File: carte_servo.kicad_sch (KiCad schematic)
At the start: 37 parts, among them J16 Conn_01x04_Male, J17 Conn_01x04_Male, J2 Conn_02x04_Top_Bottom, J24 Conn_LEDs, P1 USB_C_Plug_USB2.0, SW1 CK_KMS2xxG, U1 XGZP6897D_differential_pressu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, U2 XGZP6897D_differential_pressu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, U6 SN65HVD230, U7 LD1117S33TR_SOT223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

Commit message: small stuff
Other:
- sheet Servos ports: added GND; removed GND_SERVO
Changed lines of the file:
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@@
 	(label "Pressure_2"
 		(at 83.82 127 180)
-		(fields_autoplaced yes)
 		(effects
 			(font
@@
 	(label "Pressure_1"
 		(at 82.55 100.33 180)
-		(fields_autoplaced yes)
 		(effects
 			(font
@@
 			)
 		)
-		(pin "GND_SERVO" input
-			(at 257.81 46.99 270)
+		(pin "SERVO_POWER_1" input
+			(at 226.06 38.1 180)
 			(effects
 				(font
@@
 			)
 		)
-		(pin "SERVO_POWER_1" input
-			(at 226.06 38.1 180)
+		(pin "GND" input
+			(at 257.81 46.99 270)
 			(effects
 				(font

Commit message: add DCDC 5V
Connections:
- no-connect marks 7 -> 8
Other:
- added sheet DCDC_5V (DCDC_5V.kicad_sch)
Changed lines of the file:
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@@
 	)
 	(no_connect
+		(at 312.42 101.6)
+	)
+	(no_connect
 		(at 38.1 63.5)
 	)
@@
 	(wire
 		(pts
+			(xy 344.17 109.22) (xy 344.17 107.95)
+		)
+		(stroke
+			(width 0)
+			(type default)
+		)
+	)
+	(wire
+		(pts
 			(xy 111.76 86.36) (xy 111.76 95.25)
 		)
@@
 	(wire
 		(pts
+			(xy 356.87 97.79) (xy 353.06 97.79)
+		)
+		(stroke
+			(width 0)
+			(type default)
+		)
+	)
+	(wire
+		(pts
 			(xy 93.98 113.03) (xy 87.63 113.03)
 		)
@@
 	(wire
 		(pts
+			(xy 308.61 95.25) (xy 312.42 95.25)
+		)
+		(stroke
+			(width 0)
+			(type default)
+		)
+	)
+	(wire
+		(pts
 			(xy 210.82 50.8) (xy 210.82 53.34)
 		)
@@
 		)
 	)
+	(global_label "5V"
+		(shape output)
+		(at 356.87 97.79 0)
+		(fields_autoplaced yes)
+		(effects
+			(font
+				(size 1.27 1.27)
+			)
+			(justify left)
+		)
+		(property "Intersheetrefs" "${INTERSHEET_REFS}"
+			(at 362.1533 97.79 0)
+			(effects
+				(font
+					(size 1.27 1.27)
+				)
+				(justify left)
+				(hide yes)
+			)
+		)
+	)
 	(global_label "SDA"
 		(shape bidirectional)
@@
 	(global_label "GND"
 		(shape input)
+		(at 344.17 109.22 270)
+		(fields_autoplaced yes)
+		(effects
+			(font
+				(size 1.27 1.27)
+			)
+			(justify right)
+		)
+		(property "Intersheetrefs" "${INTERSHEET_REFS}"
+			(at 344.17 116.0757 90)
+			(effects
+				(font
+					(size 1.27 1.27)
+				)
+				(justify right)
+				(hide yes)
+			)
+		)
+	)
+	(global_label "GND"
+		(shape input)
 		(at 115.57 121.92 0)
 		(fields_autoplaced yes)
@@
 		)
 	)
+	(global_label "BATT_12V"
+		(shape input)
+		(at 308.61 95.25 180)
+		(fields_autoplaced yes)
+		(effects
+			(font
+				(size 1.27 1.27)
+			)
+			(justify right)
+		)
+		(property "Intersheetrefs" "${INTERSHEET_REFS}"
+			(at 296.8558 95.25 0)
+			(effects
+				(font
+					(size 1.27 1.27)
+				)
+				(justify right)
+				(hide yes)
+			)
+		)
+	)
 	(global_label "SERVO_1"
 		(shape output)
@@
 				)
 			)
+		)
+	)
+	(sheet
+		(at 312.42 90.17)
+		(size 40.64 17.78)
+		(fields_autoplaced yes)
+		(stroke
+			(width 0.1524)
+			(type solid)
+		)
+		(fill
+			(color 0 0 0 0.0000)
+		)
+		(property "Sheetname" "DCDC_5V"
+			(at 312.42 89.4584 0)
+			(effects
+				(font
+					(size 1.27 1.27)
+				)
+				(justify left bottom)
+			)
+		)
+		(property "Sheetfile" "DCDC_5V.kicad_sch"
+			(at 312.42 108.5346 0)
+			(effects
+				(font
+					(size 1.27 1.27)
+				)
+				(justify left top)
+			)
+		)
+		(pin "Vin" input
+			(at 312.42 95.25 180)
+			(effects
+				(font
+					(size 1.27 1.27)
+				)
+				(justify left)
+			)
+		)
+		(pin "GND" input
+			(at 344.17 107.95 270)
+			(effects
+				(font
+					(size 1.27 1.27)
+				)
+				(justify left)
+			)
+		)
+		(pin "enable" input
+			(at 312.42 101.6 180)
+			(effects
+				(font
+					(size 1.27 1.27)
+				)
+				(justify left)
+			)
+		)
+		(pin "Vout_5V" output
+			(at 353.06 97.79 0)
+			(effects
+				(font
+					(size 1.27 1.27)
+				)
+				(justify right)
+			)
+		)
+		(instances
+			(project "carte_servo"
+				(path "/e63e39d7-6ac0-4ffd-8aa3-1841a4541b55"
+					(page "9")
+				)
+			)

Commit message: add ESD diodes for USB
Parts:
- added D2, D3: ESD321, Diode_SMD:D_SOD-523, symbol Device:D_Zener
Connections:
- net D+: now also D2.1 (K)
- net D-: now also D3.1 (K)
- net GND: now also D2.2 (A), D3.2 (A)
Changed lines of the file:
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@@
 	)
 	(junction
+		(at 613.41 54.61)
+		(diameter 0)
+		(color 0 0 0 0)
+	)
+	(junction
 		(at 229.87 53.34)
 		(diameter 0)
@@
 	(wire
 		(pts
-			(xy 109.22 153.67) (xy 111.76 153.67)
+			(xy 593.09 41.91) (xy 598.17 41.91)
 		)
 		(stroke
@@
 	(wire
 		(pts
-			(xy 314.96 10.16) (xy 331.47 10.16)
+			(xy 109.22 153.67) (xy 111.76 153.67)
 		)
 		(stroke
@@
 	(wire
 		(pts
-			(xy 171.45 34.29) (xy 179.07 34.29)
+			(xy 314.96 10.16) (xy 331.47 10.16)
 		)
 		(stroke
@@
 	(wire
 		(pts
-			(xy 391.16 31.75) (xy 396.24 31.75)
+			(xy 171.45 34.29) (xy 179.07 34.29)
 		)
 		(stroke
@@
 	(wire
 		(pts
-			(xy 593.09 36.83) (xy 598.17 36.83)
+			(xy 391.16 31.75) (xy 396.24 31.75)
 		)
 		(stroke
@@
 	(wire
 		(pts
+			(xy 593.09 36.83) (xy 598.17 36.83)
+		)
+		(stroke
+			(width 0)
+			(type default)
+		)
+	)
+	(wire
+		(pts
 			(xy 391.16 82.55) (xy 396.24 82.55)
 		)
@@
 	(wire
 		(pts
+			(xy 613.41 54.61) (xy 613.41 58.42)
+		)
+		(stroke
+			(width 0)
+			(type default)
+		)
+	)
+	(wire
+		(pts
 			(xy 608.33 31.75) (xy 608.33 36.83)
 		)
@@
 	(wire
 		(pts
+			(xy 607.06 54.61) (xy 613.41 54.61)
+		)
+		(stroke
+			(width 0)
+			(type default)
+		)
+	)
+	(wire
+		(pts
 			(xy 473.71 0) (xy 480.06 0)
 		)
@@
 	(wire
 		(pts
+			(xy 613.41 54.61) (xy 619.76 54.61)
+		)
+		(stroke
+			(width 0)
+			(type default)
+		)
+	)
+	(wire
+		(pts
 			(xy 111.76 86.36) (xy 111.76 95.25)
 		)
@@
 	(wire
 		(pts
-			(xy 593.09 41.91) (xy 598.17 41.91)
-		)
-		(stroke
-			(width 0)
-			(type default)
-		)
-	)
-	(wire
-		(pts
 			(xy 125.73 182.88) (xy 127 182.88)
 		)
@@
 		)
 	)
+	(global_label "D-"
+		(shape bidirectional)
+		(at 619.76 46.99 0)
+		(fields_autoplaced yes)
+		(effects
+			(font
+				(size 1.27 1.27)
+			)
+			(justify left)
+		)
+		(property "Intersheetrefs" "${INTERSHEET_REFS}"
+			(at 625.5876 46.99 0)
+			(effects
+				(font
+					(size 1.27 1.27)
+				)
+				(justify left)
+				(hide yes)
+			)
+		)
+	)
 	(global_label "ENABLE_SERVO_POWER_1"
 		(shape input)
@@
 		)
 	)
+	(global_label "GND"
+		(shape input)
+		(at 613.41 58.42 0)
+		(fields_autoplaced yes)
+		(effects
+			(font
+				(size 1.27 1.27)
+			)
+			(justify left)
+		)
+		(property "Intersheetrefs" "${INTERSHEET_REFS}"
+			(at 620.2657 58.42 0)
+			(effects
+				(font
+					(size 1.27 1.27)
+				)
+				(justify left)
+				(hide yes)
+			)
+		)
+	)
 	(global_label "GND_POWER"
 		(shape input)
@@
 		)
 	)
+	(global_label "D+"
+		(shape bidirectional)
+		(at 607.06 46.99 0)
+		(fields_autoplaced yes)
+		(effects
+			(font
+				(size 1.27 1.27)
+			)
+			(justify left)
+		)
+		(property "Intersheetrefs" "${INTERSHEET_REFS}"
+			(at 612.8876 46.99 0)
+			(effects
+				(font
+					(size 1.27 1.27)
+				)
+				(justify left)
+				(hide yes)
+			)
+		)
+	)
 	(global_label "3.3V"
 		(shape input)
@@
 	)
 	(symbol
+		(lib_id "Device:D_Zener")
+		(at 607.06 50.8 270)
+		(unit 1)
+		(exclude_from_sim no)
+		(in_bom yes)
+		(on_board yes)
+		(dnp no)
+		(fields_autoplaced yes)
+		(property "Reference" "D2"
+			(at 609.6 49.5299 90)
+			(effects
+				(font
+					(size 1.27 1.27)
+				)
+				(justify left)
+			)
+		)
+		(property "Value" "ESD321"
+			(at 609.6 52.0699 90)
+			(effects
+				(font
+					(size 1.27 1.27)
+				)
+				(justify left)
+			)
+		)
+		(property "Footprint" "Diode_SMD:D_SOD-523"
+			(at 607.06 50.8 0)
+			(effects
+				(font
+					(size 1.27 1.27)
+				)
+				(hide yes)
+			)
+		)
+		(property "Datasheet" "https://www.mouser.fr/ProductDetail/Texas-Instruments/ESD321DYAR?qs=rQFj71Wb1eXoYwRMra0IYA%3D%3D"
+			(at 607.06 50.8 0)
+			(effects
+				(font
+					(size 1.27 1.27)
+				)
+				(hide yes)
+			)
+		)
+		(property "Description" "Zener diode"
+			(at 607.06 50.8 0)
+			(effects
+				(font
+					(size 1.27 1.27)
+				)
+				(hide yes)
+			)
+		)
+		(pin "2"
+		)
+		(pin "1"
+		)
+		(instances
+			(project "carte_servo"
+				(path "/e63e39d7-6ac0-4ffd-8aa3-1841a4541b55"
+					(reference "D2")
+					(unit 1)
+				)
+			)
+		)
+	)
+	(symbol
 		(lib_id "Connector:Conn_01x04_Male")
 		(at 39.37 158.75 0)
@@
 					(unit 1)
 				)
+			)
+		)
+	)
+	(symbol
+		(lib_id "Device:D_Zener")
+		(at 619.76 50.8 270)
+		(unit 1)
+		(exclude_from_sim no)
+		(in_bom yes)
+		(on_board yes)
+		(dnp no)
+		(fields_autoplaced yes)
+		(property "Reference" "D3"
+			(at 622.3 49.5299 90)
+			(effects
+				(font
+					(size 1.27 1.27)
+				)
+				(justify left)
+			)
+		)
+		(property "Value" "ESD321"
+			(at 622.3 52.0699 90)
+			(effects
+				(font
+					(size 1.27 1.27)
+				)
+				(justify left)
+			)
+		)
+		(property "Footprint" "Diode_SMD:D_SOD-523"
+			(at 619.76 50.8 0)
+			(effects
+				(font
+					(size 1.27 1.27)
+				)
+				(hide yes)
+			)
+		)
+		(property "Datasheet" "https://www.mouser.fr/ProductDetail/Texas-Instruments/ESD321DYAR?qs=rQFj71Wb1eXoYwRMra0IYA%3D%3D"
+			(at 619.76 50.8 0)
+			(effects
+				(font
+					(size 1.27 1.27)
+				)
+				(hide yes)
+			)
+		)
+		(property "Description" "Zener diode"
+			(at 619.76 50.8 0)
+			(effects
+				(font
+					(size 1.27 1.27)
+				)
+				(hide yes)
+			)
+		)
+		(pin "2"
+		)
+		(pin "1"
+		)
+		(instances
+			(project "carte_servo"
+				(path "/e63e39d7-6ac0-4ffd-8aa3-1841a4541b55"
+					(reference "D3")
+					(unit 1)
+				)

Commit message: fix warnings + separate enable for Steppers
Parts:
- removed C8: C_Polarized, Capacitor_THT:CP_Radial_D10.0mm_P5.00mm, symbol Device:C_Polarized
- added R37: 0R, Resistor_SMD:R_0603_1608Metric, symbol Device:R_Small
- R12: value 0R -> NC
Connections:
- net ENABLE_SERVO_POWER_2 is gone; now on net ENABLE_SERVO_POWER_1: R12.1, U8.36 (U0RXD/GPIO44/CLK_OUT2)
- net ENABLE_SERVO_POWER_1: no longer R12.2
- net sense_5V: now also R37.2
- new net ENABLE_STEPPER_POWER: R12.2, R37.1
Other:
- note removed: "todo: générer du 5V"

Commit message: change fuse + start servo order + routing
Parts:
- F1: footprint Resistor_THT:R_Axial_DIN0411_L9.9mm_D3.6mm_P15.24mm_Horizontal -> Fuse:Fuse_Littelfuse-NANO2-451_453
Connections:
- net DIR_1: now also U8.20 (GPIO12/TOUCH12/ADC2_CH1/FSPICLK/FSPIIO6/SUBSPICLK); no longer U8.28 (SPIIO6/GPIO35/FSPID/SUBSPID)
- net DIR_2: now also U8.18 (GPIO10/TOUCH10/ADC1_CH9/FSPICS0/FSPIIO4/SUBSPICS0); no longer U8.31 (GPIO38/FSPIWP/SUBSPIWP)
- net LEDs: now also U8.6 (GPIO6/TOUCH6/ADC1_CH5); no longer U8.30 (SPIDQS/GPIO37/FSPIQ/SUBSPIQ)
- net SERVO_1: now also U8.34 (MTDI/GPIO41/CLK_OUT1); no longer U8.12 (GPIO8/TOUCH8/ADC1_CH7/SUBSPICS1)
- net SERVO_2: now also U8.28 (SPIIO6/GPIO35/FSPID/SUBSPID); no longer U8.18 (GPIO10/TOUCH10/ADC1_CH9/FSPICS0/FSPIIO4/SUBSPICS0)
- net SERVO_3: now also U8.30 (SPIDQS/GPIO37/FSPIQ/SUBSPIQ); no longer U8.19 (GPIO11/TOUCH11/ADC2_CH0/FSPID/FSPIIO5/SUBSPID)
- net SERVO_7: now also U8.29 (SPIIO7/GPIO36/FSPICLK/SUBSPICLK); no longer U8.20 (GPIO12/TOUCH12/ADC2_CH1/FSPICLK/FSPIIO6/SUBSPICLK)
- net SERVO_8: now also U8.37 (U0TXD/GPIO43/CLK_OUT1); no longer U8.6 (GPIO6/TOUCH6/ADC1_CH5), U8.9 (GPIO16/U0CTS/ADC2_CH5/XTAL_32K_N)
- net STEP_1: now also U8.12 (GPIO8/TOUCH8/ADC1_CH7/SUBSPICS1); no longer U8.29 (SPIIO7/GPIO36/FSPICLK/SUBSPICLK)
- net STEP_2: now also U8.19 (GPIO11/TOUCH11/ADC2_CH0/FSPID/FSPIIO5/SUBSPID); no longer U8.34 (MTDI/GPIO41/CLK_OUT1)
- net TRANSISTOR_3: now also U8.9 (GPIO16/U0CTS/ADC2_CH5/XTAL_32K_N); no longer U8.37 (U0TXD/GPIO43/CLK_OUT1)
- net CAN_H renamed CAN+
- net CAN_L renamed CAN-

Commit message: continue routing
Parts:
- added C8: 100nF, Capacitor_SMD:C_0603_1608Metric, symbol Device:C
- C11: value 100nF -> 4.7µF
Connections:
- net 3.3V: now also C11.1
- net GND: now also C8.2
- net Pressure_2: now also U8.38 (GPIO2/TOUCH2/ADC1_CH1), C8.1; no longer C11.1, U8.5 (GPIO5/TOUCH5/ADC1_CH4)
- net SERVO_1: now also U8.28 (SPIIO6/GPIO35/FSPID/SUBSPID); no longer U8.34 (MTDI/GPIO41/CLK_OUT1)
- net SERVO_2: now also U8.29 (SPIIO7/GPIO36/FSPICLK/SUBSPICLK); no longer U8.28 (SPIIO6/GPIO35/FSPID/SUBSPID)
- net SERVO_4: now also U8.32 (MTCK/GPIO39/CLK_OUT3/SUBSPICS1); no longer U8.35 (MTMS/GPIO42)
- net SERVO_6: now also U8.34 (MTDI/GPIO41/CLK_OUT1); no longer U8.32 (MTCK/GPIO39/CLK_OUT3/SUBSPICS1)
- net SERVO_7: now also U8.35 (MTMS/GPIO42); no longer U8.29 (SPIIO7/GPIO36/FSPICLK/SUBSPICLK)
- net STEP_1: now also U8.19 (GPIO11/TOUCH11/ADC2_CH0/FSPID/FSPIIO5/SUBSPID); no longer U8.12 (GPIO8/TOUCH8/ADC1_CH7/SUBSPICS1)
- net STEP_2: now also U8.12 (GPIO8/TOUCH8/ADC1_CH7/SUBSPICS1); no longer U8.19 (GPIO11/TOUCH11/ADC2_CH0/FSPID/FSPIIO5/SUBSPID)
- net sense_5V: now also U8.5 (GPIO5/TOUCH5/ADC1_CH4); no longer U8.38 (GPIO2/TOUCH2/ADC1_CH1)

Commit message: basic routing
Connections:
- net DIR_2: now also U8.6 (GPIO6/TOUCH6/ADC1_CH5); no longer U8.18 (GPIO10/TOUCH10/ADC1_CH9/FSPICS0/FSPIIO4/SUBSPICS0)
- net LEDs: now also U8.18 (GPIO10/TOUCH10/ADC1_CH9/FSPICS0/FSPIIO4/SUBSPICS0); no longer U8.6 (GPIO6/TOUCH6/ADC1_CH5)
- net SCL: no longer U2.7 (SCL)
- net SDA: no longer U2.6 (SDA)
- no-connect marks 8 -> 10
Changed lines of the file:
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@@
 	)
 	(no_connect
+		(at 107.95 127)
+	)
+	(no_connect
 		(at 331.47 12.7)
 	)
@@
 	)
 	(no_connect
+		(at 107.95 124.46)
+	)
+	(no_connect
 		(at 487.68 80.01)
 	)
@@
 	(wire
 		(pts
-			(xy 107.95 127) (xy 115.57 127)
-		)
-		(stroke
-			(width 0)
-			(type default)
-		)
-	)
-	(wire
-		(pts
 			(xy 355.6 10.16) (xy 351.79 10.16)
 		)
@@
 	(wire
 		(pts
-			(xy 107.95 124.46) (xy 115.57 124.46)
-		)
-		(stroke
-			(width 0)
-			(type default)
-		)
-	)
-	(wire
-		(pts
 			(xy 125.73 177.8) (xy 127 177.8)
 		)
@@
 	(label "Pressure_2"
 		(at 83.82 127 180)
+		(fields_autoplaced yes)
 		(effects
 			(font
@@
 	(label "Pressure_1"
 		(at 82.55 100.33 180)
+		(fields_autoplaced yes)
 		(effects
 			(font
@@
 		)
 	)
+	(global_label "LEDs"
+		(shape output)
+		(at 494.03 54.61 0)
+		(fields_autoplaced yes)
+		(effects
+			(font
+				(size 1.27 1.27)
+			)
+			(justify left)
+		)
+		(property "Intersheetrefs" "${INTERSHEET_REFS}"
+			(at 501.4904 54.61 0)
+			(effects
+				(font
+					(size 1.27 1.27)
+				)
+				(justify left)
+				(hide yes)
+			)
+		)
+	)
 	(global_label "5V"
 		(shape input)
@@
 		)
 	)
-	(global_label "SDA"
-		(shape input)
-		(at 115.57 127 0)
-		(fields_autoplaced yes)
-		(effects
-			(font
-				(size 1.27 1.27)
-			)
-			(justify left)
-		)
-		(property "Intersheetrefs" "${INTERSHEET_REFS}"
-			(at 121.5512 126.9206 0)
-			(effects
-				(font
-					(size 1.27 1.27)
-				)
-				(justify left)
-				(hide yes)
-			)
-		)
-	)
 	(global_label "SERVO_6"
 		(shape output)
@@
 		)
 	)
-	(global_label "DIR_2"
-		(shape output)
-		(at 494.03 54.61 0)
-		(fields_autoplaced yes)
-		(effects
-			(font
-				(size 1.27 1.27)
-			)
-			(justify left)
-		)
-		(property "Intersheetrefs" "${INTERSHEET_REFS}"
-			(at 502.3371 54.61 0)
-			(effects
-				(font
-					(size 1.27 1.27)
-				)
-				(justify left)
-				(hide yes)
-			)
-		)
-	)
 	(global_label "GND"
 		(shape input)
@@
 		)
 	)
+	(global_label "DIR_2"
+		(shape output)
+		(at 494.03 44.45 0)
+		(fields_autoplaced yes)
+		(effects
+			(font
+				(size 1.27 1.27)
+			)
+			(justify left)
+		)
+		(property "Intersheetrefs" "${INTERSHEET_REFS}"
+			(at 502.3371 44.45 0)
+			(effects
+				(font
+					(size 1.27 1.27)
+				)
+				(justify left)
+				(hide yes)
+			)
+		)
+	)
 	(global_label "12V_POW_P"
 		(shape input)
@@
 		)
 	)
-	(global_label "CAN+"
-		(shape bidirectional)
-		(at 355.6 10.16 0)
+	(global_label "STEP_2"
+		(shape output)
+		(at 494.03 49.53 0)
 		(fields_autoplaced yes)
 		(effects
@@
 		)
 		(property "Intersheetrefs" "${INTERSHEET_REFS}"
-			(at 364.958 10.16 0)
+			(at 503.7884 49.53 0)
 			(effects
 				(font
@@
 		)
 	)
-	(global_label "LEDs"
-		(shape output)
-		(at 494.03 44.45 0)
+	(global_label "CAN+"
+		(shape bidirectional)
+		(at 355.6 10.16 0)
 		(fields_autoplaced yes)
 		(effects
@@
 		)
 		(property "Intersheetrefs" "${INTERSHEET_REFS}"
-			(at 501.4904 44.45 0)
+			(at 364.958 10.16 0)
 			(effects
 				(font
@@
 		)
 	)
-	(global_label "SCL"
-		(shape input)
-		(at 115.57 124.46 0)
-		(fields_autoplaced yes)
-		(effects
-			(font
-				(size 1.27 1.27)
-			)
-			(justify left)
-		)
-		(property "Intersheetrefs" "${INTERSHEET_REFS}"
-			(at 121.4907 124.3806 0)
-			(effects
-				(font
-					(size 1.27 1.27)
-				)
-				(justify left)
-				(hide yes)
-			)
-		)
-	)
 	(global_label "SERVO_5"
 		(shape output)
@@
 				(hide yes)
 			)
-		)
-	)
-	(global_label "STEP_2"
-		(shape output)
-		(at 494.03 49.53 0)
-		(fields_autoplaced yes)
-		(effects
-			(font
-				(size 1.27 1.27)
-			)
-			(justify left)
-		)
-		(property "Intersheetrefs" "${INTERSHEET_REFS}"
-			(at 503.7884 49.53 0)
-			(effects
-				(font
-					(size 1.27 1.27)
-				)
-				(justify left)
-				(hide yes)
-			)

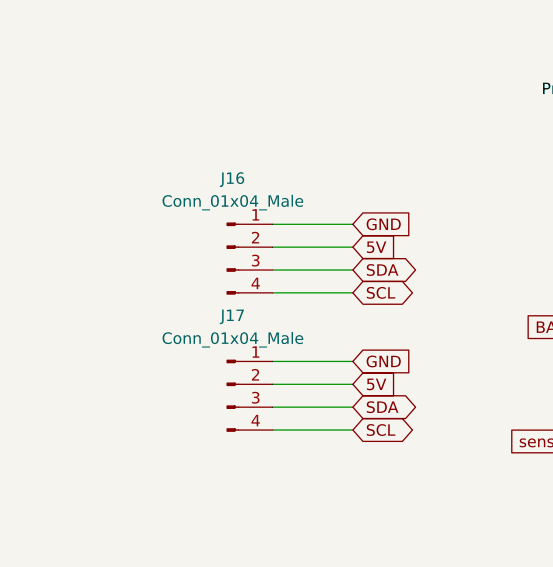
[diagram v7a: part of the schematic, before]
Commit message: widen 12V/5V
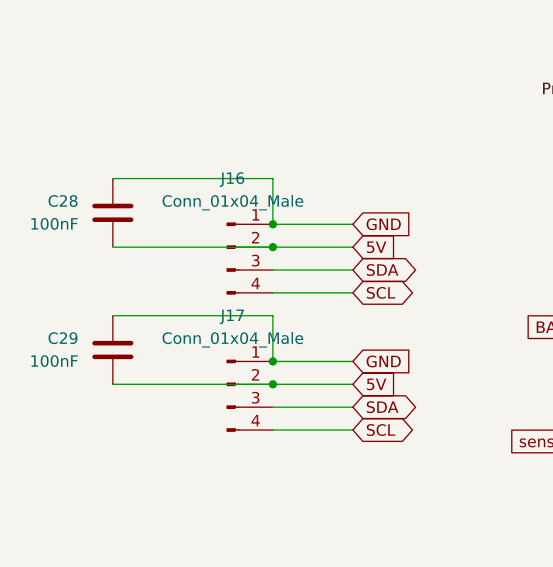
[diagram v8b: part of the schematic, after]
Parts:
- added C28, C29: 100nF, Capacitor_SMD:C_0805_2012Metric, symbol Device:C
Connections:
- net 5V: now also C28.2, C29.2
- net GND: now also C28.1, C29.1
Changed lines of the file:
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@@
 	)
 	(junction
+		(at 44.45 143.51)
+		(diameter 0)
+		(color 0 0 0 0)
+	)
+	(junction
 		(at 110.49 154.94)
 		(diameter 0)
@@
 	)
 	(junction
+		(at 44.45 156.21)
+		(diameter 0)
+		(color 0 0 0 0)
+	)
+	(junction
 		(at 87.63 124.46)
 		(diameter 0)
@@
 	)
 	(junction
+		(at 44.45 140.97)
+		(diameter 0)
+		(color 0 0 0 0)
+	)
+	(junction
 		(at 196.85 151.13)
 		(diameter 0)
@@
 		(color 0 0 0 0)
 	)
+	(junction
+		(at 44.45 158.75)
+		(diameter 0)
+		(color 0 0 0 0)
+	)
 	(no_connect
 		(at 59.69 63.5)
@@
 	(wire
 		(pts
+			(xy 26.67 151.13) (xy 44.45 151.13)
+		)
+		(stroke
+			(width 0)
+			(type default)
+		)
+	)
+	(wire
+		(pts
 			(xy 391.16 29.21) (xy 396.24 29.21)
 		)
@@
 	(wire
 		(pts
+			(xy 26.67 158.75) (xy 44.45 158.75)
+		)
+		(stroke
+			(width 0)
+			(type default)
+		)
+	)
+	(wire
+		(pts
+			(xy 44.45 135.89) (xy 44.45 140.97)
+		)
+		(stroke
+			(width 0)
+			(type default)
+		)
+	)
+	(wire
+		(pts
 			(xy 107.95 121.92) (xy 111.76 121.92)
 		)
@@
 	(wire
 		(pts
-			(xy 44.45 143.51) (xy 53.34 143.51)
+			(xy 41.91 66.04) (xy 39.37 66.04)
 		)
 		(stroke
@@
 	(wire
 		(pts
-			(xy 41.91 66.04) (xy 39.37 66.04)
+			(xy 391.16 36.83) (xy 396.24 36.83)
 		)
 		(stroke
@@
 	(wire
 		(pts
-			(xy 391.16 36.83) (xy 396.24 36.83)
+			(xy 111.76 121.92) (xy 115.57 121.92)
 		)
 		(stroke
@@
 	(wire
 		(pts
-			(xy 111.76 121.92) (xy 115.57 121.92)
+			(xy 314.96 15.24) (xy 318.77 15.24)
 		)
 		(stroke
@@
 	(wire
 		(pts
-			(xy 314.96 15.24) (xy 318.77 15.24)
+			(xy 487.68 67.31) (xy 494.03 67.31)
 		)
 		(stroke
@@
 	(wire
 		(pts
-			(xy 487.68 67.31) (xy 494.03 67.31)
+			(xy 44.45 151.13) (xy 44.45 156.21)
 		)
 		(stroke
@@
 	(wire
 		(pts
+			(xy 44.45 158.75) (xy 53.34 158.75)
+		)
+		(stroke
+			(width 0)
+			(type default)
+		)
+	)
+	(wire
+		(pts
 			(xy 326.39 15.24) (xy 331.47 15.24)
 		)
@@
 	(wire
 		(pts
-			(xy 38.1 63.5) (xy 39.37 63.5)
+			(xy 44.45 143.51) (xy 53.34 143.51)
 		)
 		(stroke
@@
 	(wire
 		(pts
-			(xy 194.31 158.75) (xy 199.39 158.75)
+			(xy 38.1 63.5) (xy 39.37 63.5)
 		)
 		(stroke
@@
 	(wire
 		(pts
-			(xy 44.45 158.75) (xy 53.34 158.75)
+			(xy 194.31 158.75) (xy 199.39 158.75)
 		)
 		(stroke
@@
 	(wire
 		(pts
+			(xy 26.67 143.51) (xy 44.45 143.51)
+		)
+		(stroke
+			(width 0)
+			(type default)
+		)
+	)
+	(wire
+		(pts
+			(xy 26.67 135.89) (xy 44.45 135.89)
+		)
+		(stroke
+			(width 0)
+			(type default)
+		)
+	)
+	(wire
+		(pts
 			(xy 323.85 60.96) (xy 335.28 60.96)
 		)
@@
 	)
 	(symbol
+		(lib_id "Device:C")
+		(at 26.67 154.94 0)
+		(mirror y)
+		(unit 1)
+		(exclude_from_sim no)
+		(in_bom yes)
+		(on_board yes)
+		(dnp no)
+		(property "Reference" "C29"
+			(at 22.86 153.6699 0)
+			(effects
+				(font
+					(size 1.27 1.27)
+				)
+				(justify left)
+			)
+		)
+		(property "Value" "100nF"
+			(at 22.86 156.2099 0)
+			(effects
+				(font
+					(size 1.27 1.27)
+				)
+				(justify left)
+			)
+		)
+		(property "Footprint" "Capacitor_SMD:C_0805_2012Metric"
+			(at 25.7048 158.75 0)
+			(effects
+				(font
+					(size 1.27 1.27)
+				)
+				(hide yes)
+			)
+		)
+		(property "Datasheet" "~"
+			(at 26.67 154.94 0)
+			(effects
+				(font
+					(size 1.27 1.27)
+				)
+				(hide yes)
+			)
+		)
+		(property "Description" ""
+			(at 26.67 154.94 0)
+			(effects
+				(font
+					(size 1.27 1.27)
+				)
+				(hide yes)
+			)
+		)
+		(pin "1"
+		)
+		(pin "2"
+		)
+		(instances
+			(project "carte_servo"
+				(path "/e63e39d7-6ac0-4ffd-8aa3-1841a4541b55"
+					(reference "C29")
+					(unit 1)
+				)
+			)
+		)
+	)
+	(symbol
 		(lib_id "Connector:Conn_01x04_Male")
 		(at 39.37 158.75 0)
@@
 					(unit 1)
 				)
+			)
+		)
+	)
+	(symbol
+		(lib_id "Device:C")
+		(at 26.67 139.7 0)
+		(mirror y)
+		(unit 1)
+		(exclude_from_sim no)
+		(in_bom yes)
+		(on_board yes)
+		(dnp no)
+		(property "Reference" "C28"
+			(at 22.86 138.4299 0)
+			(effects
+				(font
+					(size 1.27 1.27)
+				)
+				(justify left)
+			)
+		)
+		(property "Value" "100nF"
+			(at 22.86 140.9699 0)
+			(effects
+				(font
+					(size 1.27 1.27)
+				)
+				(justify left)
+			)
+		)
+		(property "Footprint" "Capacitor_SMD:C_0805_2012Metric"
+			(at 25.7048 143.51 0)
+			(effects
+				(font
+					(size 1.27 1.27)
+				)
+				(hide yes)
+			)
+		)
+		(property "Datasheet" "~"
+			(at 26.67 139.7 0)
+			(effects
+				(font
+					(size 1.27 1.27)
+				)
+				(hide yes)
+			)
+		)
+		(property "Description" ""
+			(at 26.67 139.7 0)
+			(effects
+				(font
+					(size 1.27 1.27)
+				)
+				(hide yes)
+			)
+		)
+		(pin "1"
+		)
+		(pin "2"
+		)
+		(instances
+			(project "carte_servo"
+				(path "/e63e39d7-6ac0-4ffd-8aa3-1841a4541b55"
+					(reference "C28")
+					(unit 1)
+				)
